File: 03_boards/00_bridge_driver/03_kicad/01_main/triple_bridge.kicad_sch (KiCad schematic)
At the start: 3 parts, among them U1 IR2104, U2 IR2104, U3 IR2104

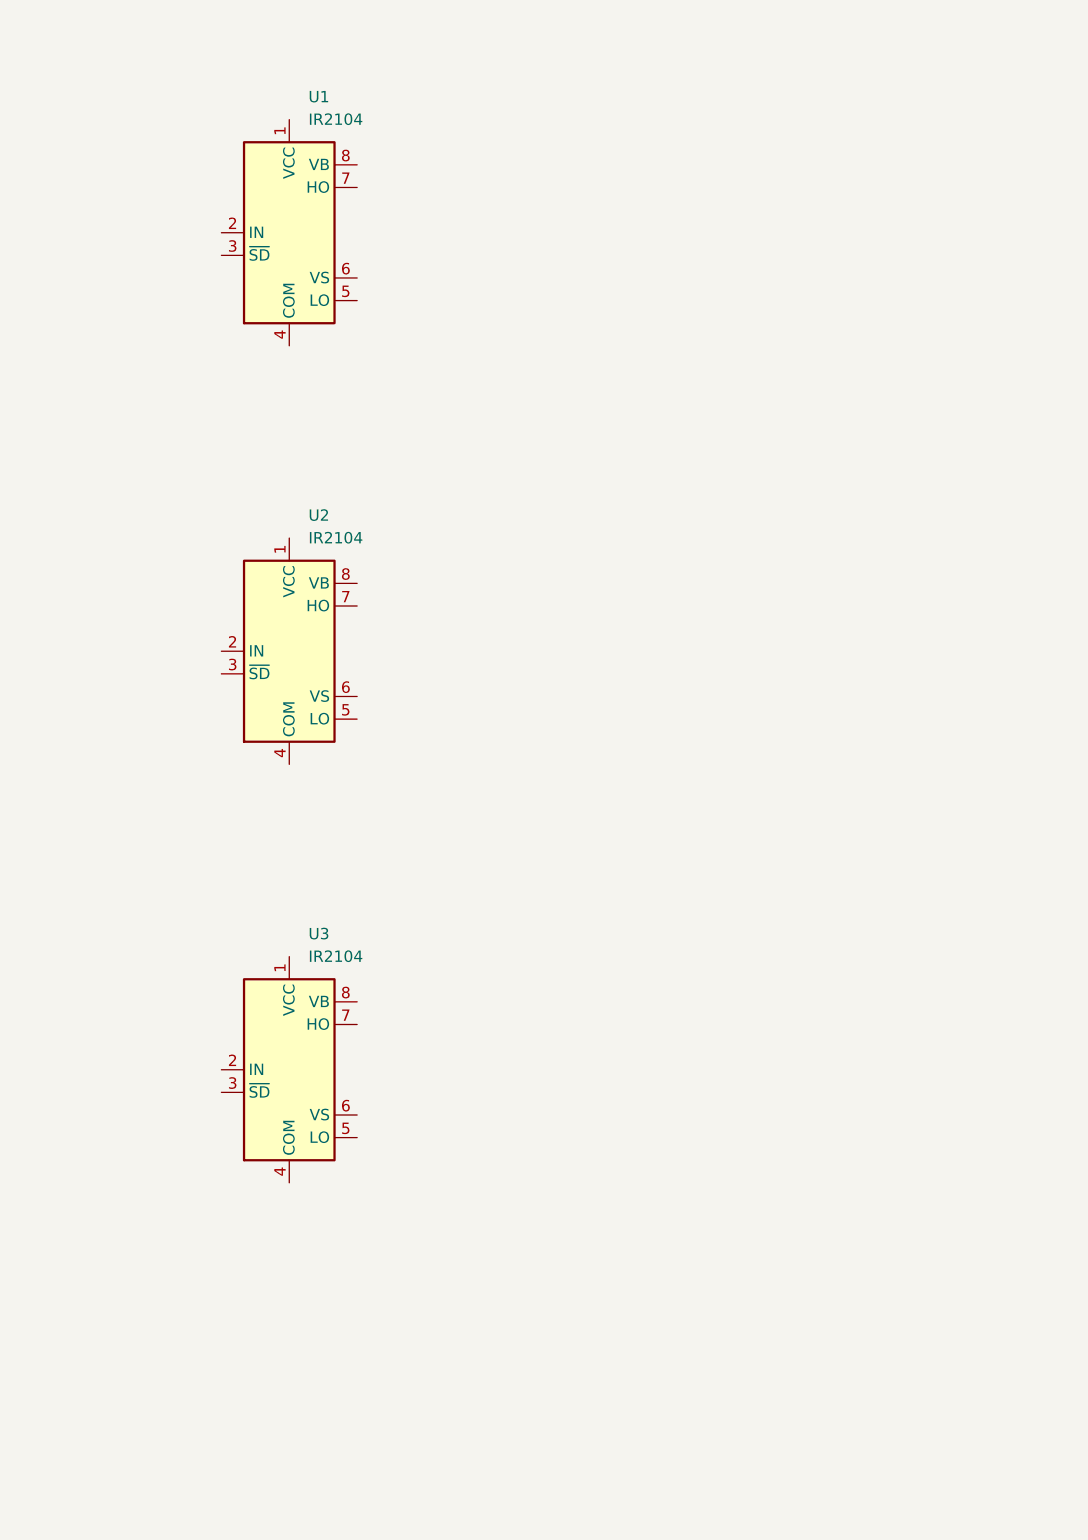
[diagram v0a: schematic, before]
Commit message: Beginning work on triple bridge driver
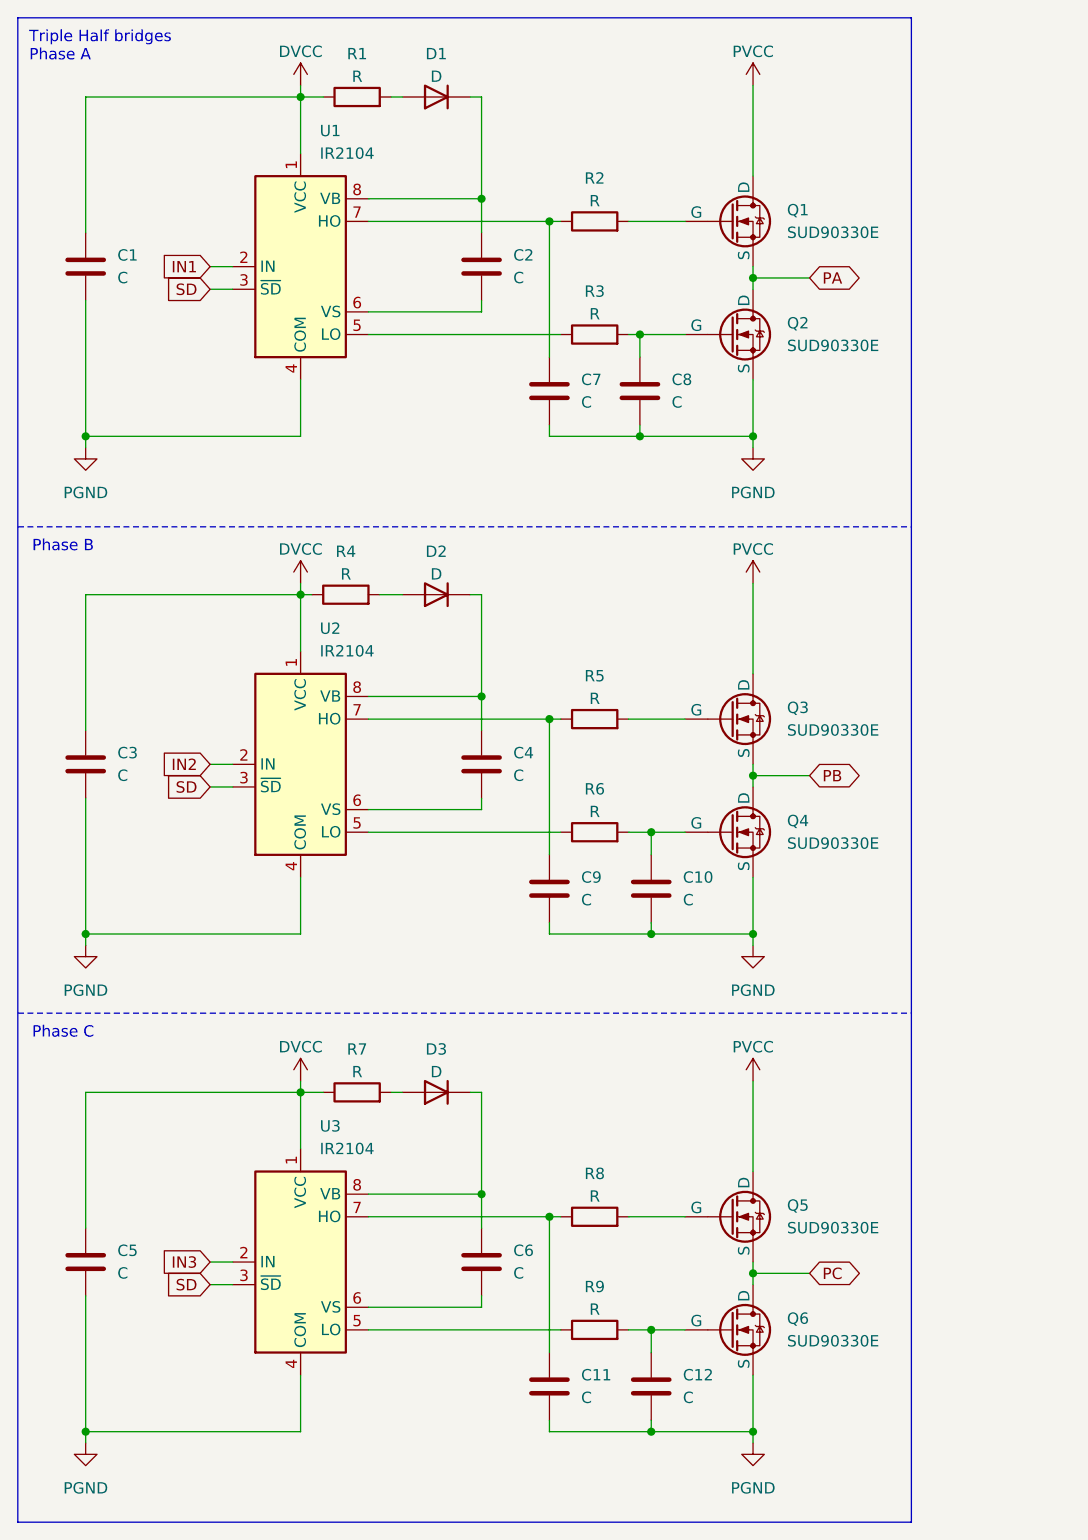
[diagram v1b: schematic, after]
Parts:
- added C1, C10, C11, C12, C2, C3, C4, C5, C6, C7, C8, C9: C, symbol Device:C
- added D1, D2, D3: D, symbol Device:D
- added Q1, Q2, Q3, Q4, Q5, Q6: SUD90330E, symbol Simulation_SPICE:NMOS
- added R1, R2, R3, R4, R5, R6, R7, R8, R9: R, symbol Device:R
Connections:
- net DVCC: now reaches U3.1 (VCC)
- net DVCC: now also U1.1 (VCC), U2.1 (VCC), C1.1, C3.1, C5.1, R1.1, R4.1, R7.1
- net IN3: now reaches U3.2 (IN)
- net SD: now reaches U3.3 (~{SD})
- net SD: now also U1.3 (~{SD}), U2.3 (~{SD})
- net PGND: now reaches U3.4 (COM)
- net PGND: now also U1.4 (COM), U2.4 (COM), C1.2, C10.2, C11.2, C12.2, C3.2, C5.2, C7.2, C8.2, C9.2, Q2.3 (S), Q4.3 (S), Q6.3 (S)
- net at U3.5 (LO): now also R9.1
- net at U3.6 (VS): now also C6.2
- net at U3.7 (HO): now also C11.1, R8.1
- net at U3.8 (VB): now also C6.1, D3.1 (K)
- net IN1: now reaches U1.2 (IN)
- net at U1.5 (LO): now also R3.1
- net at U1.6 (VS): now also C2.2
- net at U1.7 (HO): now also C7.1, R2.1
- net at U1.8 (VB): now also C2.1, D1.1 (K)
- net IN2: now reaches U2.2 (IN)
- net at U2.5 (LO): now also R6.1
- net at U2.6 (VS): now also C4.2
- net at U2.7 (HO): now also C9.1, R5.1
- net at U2.8 (VB): now also C4.1, D2.1 (K)
- new net: C12.1, Q6.2 (G), R9.2
- new net: D1.2 (A), R1.2
- new net: C8.1, Q2.2 (G), R3.2
- new net: Q5.2 (G), R8.2
- new net: Q1.2 (G), R2.2
- new net: C10.1, Q4.2 (G), R6.2
- new net: D3.2 (A), R7.2
- new net: D2.2 (A), R4.2
- new net: Q3.2 (G), R5.2
- new net PA: Q1.3 (S), Q2.1 (D)
- new net PB: Q3.3 (S), Q4.1 (D)
- new net PC: Q5.3 (S), Q6.1 (D)
- new net PVCC: Q1.1 (D), Q3.1 (D), Q5.1 (D)
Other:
- note added: "Phase B"
- note added: "Phase C"
- note added: "Triple Half bridges Phase A"
- title: (none) -> Triple half bridge drivers and switches
- moved on the sheet: U1

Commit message: Boot strap capacitors, resistors and diode work for triple half bridge driver
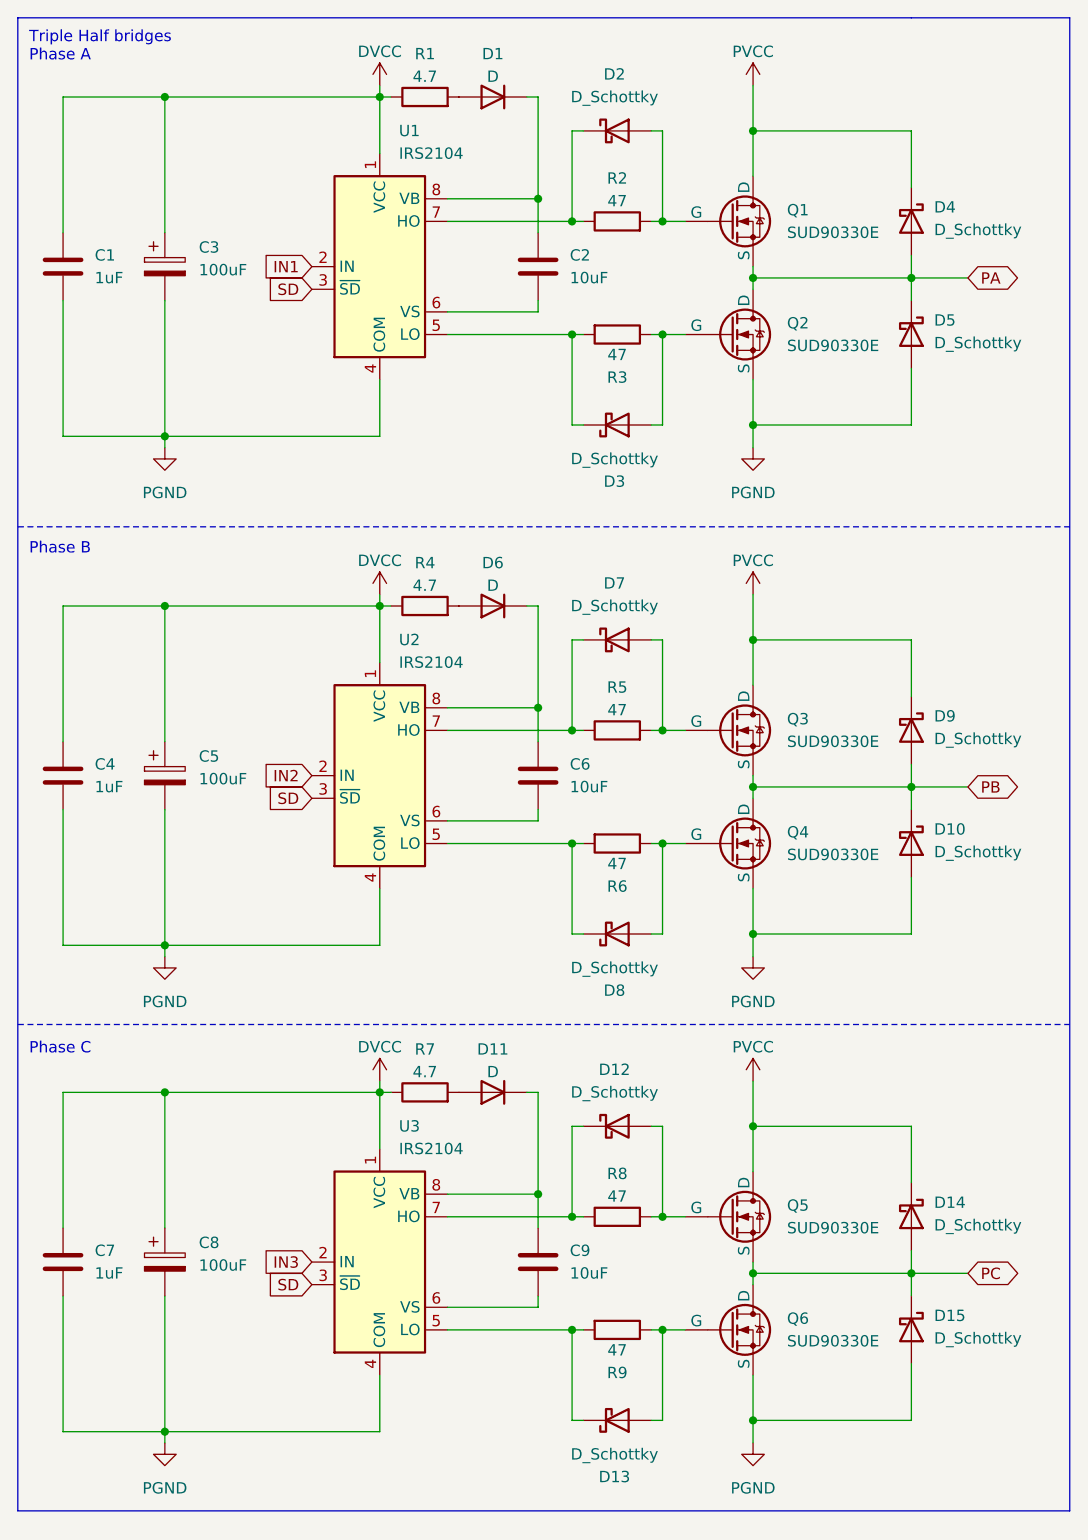
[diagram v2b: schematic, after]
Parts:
- removed C10, C11, C12, C3, C5, C8: C, symbol Device:C
- removed D2, D3: D, symbol Device:D
- added C3, C5, C8: 100uF, symbol Device:C_Polarized
- added D10, D12, D13, D14, D15, D2, D3, D4, D5, D7, D8, D9: D_Schottky, symbol Device:D_Schottky
- added D11, D6: D, symbol Device:D
- C1, C4, C7: value C -> 1uF
- C2, C6, C9: value C -> 10uF
- R1, R4, R7: value R -> 4.7
- R2, R3, R5, R6, R8, R9: value R -> 47
- U1, U2, U3: value IR2104 -> IRS2104
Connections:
- net DVCC: now also C4.1, C7.1, C3.1, C5.1, C8.1
- net PA: now also D4.2 (A), D5.1 (K)
- net PB: now also D10.1 (K), D9.2 (A)
- net PC: now also D14.2 (A), D15.1 (K)
- net PGND: now also C4.2, C3.2, C5.2, C8.2, D10.2 (A), D15.2 (A), D5.2 (A); no longer C9.2
- net PVCC: now also D14.1 (K), D4.1 (K), D9.1 (K)
- net at R9.2: now also U3.5 (LO), D13.1 (K); no longer Q6.2 (G)
- net at R8.1, U3.7 (HO): now also D12.1 (K)
- net at R6.1: now also Q4.2 (G), D8.2 (A); no longer U2.5 (LO)
- net at U2.6 (VS): now also C6.2; no longer C4.2
- net at R5.1, U2.7 (HO): now also D7.1 (K); no longer C9.1
- net at U2.8 (VB): now also C6.1, D6.1 (K); no longer C4.1
- net at Q2.2 (G): now also R3.1, D3.2 (A); no longer R3.2
- net at Q5.2 (G), R8.2: now also D12.2 (A)
- net at R2.1, U1.7 (HO): now also D2.1 (K); no longer C7.1
- net at Q1.2 (G), R2.2: now also D2.2 (A)
- net at R9.1: now also Q6.2 (G), D13.2 (A); no longer U3.5 (LO)
- net at U3.6 (VS): now also C9.2; no longer C6.2
- net at U3.8 (VB): now also C9.1, D11.1 (K); no longer C6.1
- net at R6.2: now also U2.5 (LO), D8.1 (K); no longer Q4.2 (G)
- net at R7.2: now also D11.2 (A)
- net at R4.2: now also D6.2 (A)
- net at Q3.2 (G), R5.2: now also D7.2 (A)
- net at U1.5 (LO): now also R3.2, D3.1 (K); no longer R3.1
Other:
- moved on the sheet: C1, C2, D1, R1, R2, R3, U1
